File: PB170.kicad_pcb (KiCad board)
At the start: 4 copper layers, 96.5 x 71.1 mm, 39 parts, among them J2 USB_B_Micro, Q1 P-MOSFET-MLP_HS, Q2 BC817, SW1 SW_MEC_5E, SW2 SW_MEC_5E, SW3 SW_SPDT, U1 74HC00, U2 74HC08, U3 74HC4511D, U4 HEF4518BT, U5 74HC32

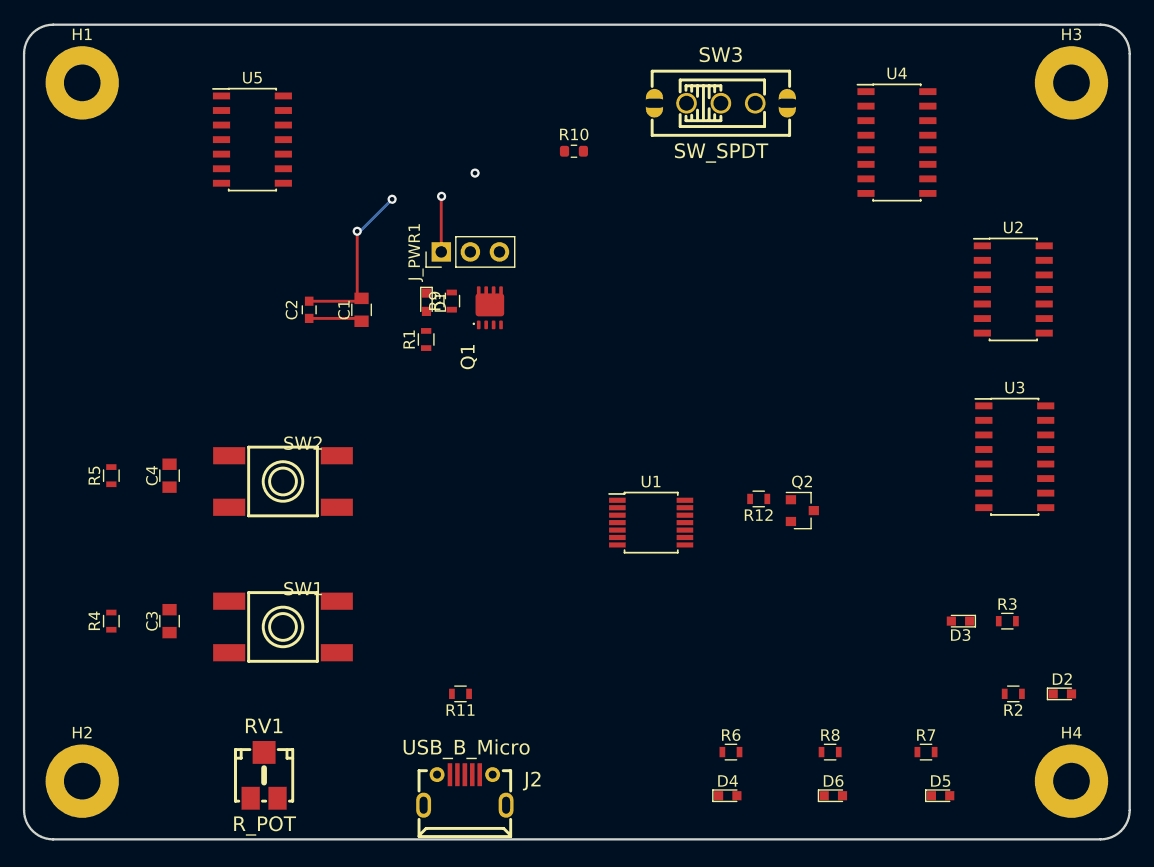
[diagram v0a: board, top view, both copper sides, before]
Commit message: Put components on board, set up 3d models of button and switch
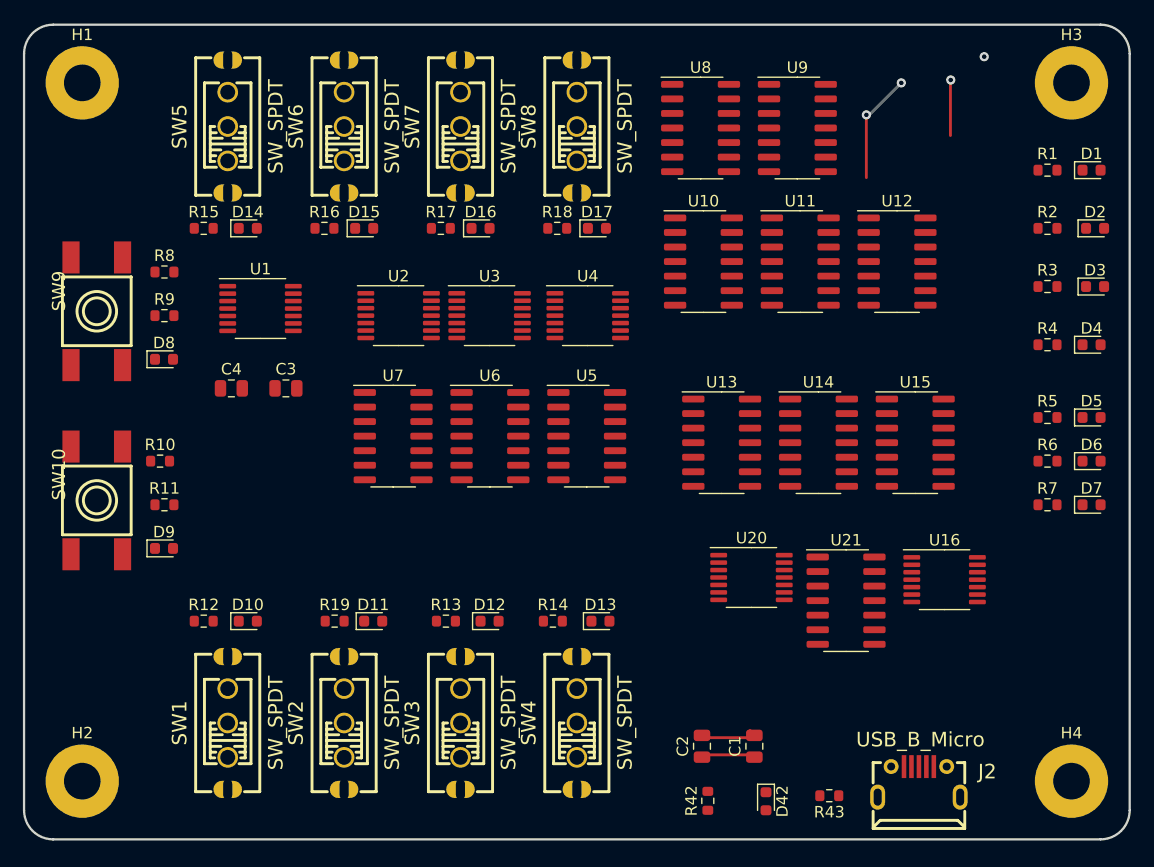
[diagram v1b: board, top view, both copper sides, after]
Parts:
- removed J_PWR1: Conn_01x03, Pin_Headers:Pin_Header_Straight_1x03_Pitch2.54mm
- removed Q1: P-MOSFET-MLP_HS, PB170:MLP3.3X3.3_HS
- removed Q2: BC817, TO_SOT_Packages_SMD:SOT-23
- removed RV1: R_POT, PB170:potentiometer10k
- added D1: LED green, LED_SMD:LED_0603_1608Metric, F.Cu at (133.8, 38.1)
- added D10: LED green, LED_SMD:LED_0603_1608Metric, F.Cu at (60.2, 77.5)
- added D11: LED green, LED_SMD:LED_0603_1608Metric, F.Cu at (71.1, 77.5)
- added D12: LED green, LED_SMD:LED_0603_1608Metric, F.Cu at (81.3, 77.5)
- added D13: LED green, LED_SMD:LED_0603_1608Metric, F.Cu at (91.0, 77.5)
- added D14: LED green, LED_SMD:LED_0603_1608Metric, F.Cu at (60.2, 43.2)
- added D15: LED green, LED_SMD:LED_0603_1608Metric, F.Cu at (70.3, 43.2)
- added D16: LED green, LED_SMD:LED_0603_1608Metric, F.Cu at (80.5, 43.2)
- added D17: LED green, LED_SMD:LED_0603_1608Metric, F.Cu at (90.7, 43.2)
- added D7: LED yellow, LED_SMD:LED_0603_1608Metric, F.Cu at (133.8, 67.3)
- added D8: LED yellow, LED_SMD:LED_0603_1608Metric, F.Cu at (52.9, 54.6)
- added D9: LED yellow, LED_SMD:LED_0603_1608Metric, F.Cu at (52.9, 71.1)
- added R1: 180R, Resistor_SMD:R_0603_1608Metric, F.Cu at (130.0, 38.1)
- added R11: 180R, Resistor_SMD:R_0603_1608Metric, F.Cu at (52.9, 67.3)
- added R13: 180R, Resistor_SMD:R_0603_1608Metric, F.Cu at (77.5, 77.5)
- added R14: 180R, Resistor_SMD:R_0603_1608Metric, F.Cu at (86.8, 77.5)
- added R15: 180R, Resistor_SMD:R_0603_1608Metric, F.Cu at (56.3, 43.2)
- added R16: 180R, Resistor_SMD:R_0603_1608Metric, F.Cu at (66.9, 43.2)
- added R17: 180R, Resistor_SMD:R_0603_1608Metric, F.Cu at (77.0, 43.2)
- added R18: 180R, Resistor_SMD:R_0603_1608Metric, F.Cu at (87.2, 43.2)
- added R19: 180R, Resistor_SMD:R_0603_1608Metric, F.Cu at (67.8, 77.5)
- added SW10: SW_MEC_5E, PB170:TactileSwitch_C381064, F.Cu at (47.0, 66.9)
- added SW4: SW_SPDT, PB170:toggleSwitch, F.Cu at (88.9, 86.4)
- added SW5: SW_SPDT, PB170:toggleSwitch, F.Cu at (58.4, 34.3)
- added SW6: SW_SPDT, PB170:toggleSwitch, F.Cu at (68.6, 34.3)
- added SW7: SW_SPDT, PB170:toggleSwitch, F.Cu at (78.7, 34.3)
- added SW8: SW_SPDT, PB170:toggleSwitch, F.Cu at (88.9, 34.3)
- added SW9: SW_MEC_5E, PB170:TactileSwitch_C381064, F.Cu at (47.0, 50.4)
- added U10: 74HC08, Package_SO:SOIC-14_3.9x8.7mm_P1.27mm, F.Cu at (100.0, 46.1)
- added U11: 74HC08, Package_SO:SOIC-14_3.9x8.7mm_P1.27mm, F.Cu at (108.4, 46.1)
- added U12: 74HC32, Package_SO:SOIC-14_3.9x8.7mm_P1.27mm, F.Cu at (116.8, 46.1)
- added U13: 74HC08, Package_SO:SOIC-14_3.9x8.7mm_P1.27mm, F.Cu at (101.5, 61.9)
- added U14: 74HC08, Package_SO:SOIC-14_3.9x8.7mm_P1.27mm, F.Cu at (110.0, 61.9)
- added U15: 74HC32, Package_SO:SOIC-14_3.9x8.7mm_P1.27mm, F.Cu at (118.4, 61.9)
- added U16: 74HC86, Package_SO:TSSOP-14_4.4x5mm_P0.65mm, F.Cu at (121.0, 73.8)
- added U20: 74HC00, Package_SO:TSSOP-14_4.4x5mm_P0.65mm, F.Cu at (104.1, 73.7)
- added U21: 74HC32, Package_SO:SOIC-14_3.9x8.7mm_P1.27mm, F.Cu at (112.4, 75.7)
- added U6: 74HC08, Package_SO:SOIC-14_3.9x8.7mm_P1.27mm, F.Cu at (81.3, 61.3)
- added U7: 74HC32, Package_SO:SOIC-14_3.9x8.7mm_P1.27mm, F.Cu at (72.9, 61.3)
- added U8: 74HC08, Package_SO:SOIC-14_3.9x8.7mm_P1.27mm, F.Cu at (99.7, 34.4)
- added U9: 74HC32, Package_SO:SOIC-14_3.9x8.7mm_P1.27mm, F.Cu at (108.2, 34.4)
- C1, C3, C4: footprint Capacitors_SMD:C_0805 -> Capacitor_SMD:C_0805_2012Metric
- C2: footprint Capacitors_SMD:C_0603 -> Capacitor_SMD:C_0805_2012Metric
- D2, D3: value LED yellow -> LED green; footprint LEDs:LED_0603 -> LED_SMD:LED_0603_1608Metric
- D4: footprint LEDs:LED_0603 -> LED_SMD:LED_0603_1608Metric
- D42: renamed from D1; footprint LEDs:LED_0603 -> LED_SMD:LED_0603_1608Metric
- D5: value LED blue -> LED red; footprint LEDs:LED_0603 -> LED_SMD:LED_0603_1608Metric
- D6: value LED white -> LED yellow; footprint LEDs:LED_0603 -> LED_SMD:LED_0603_1608Metric
- R12, R7: value 220R -> 180R; footprint Resistors_SMD:R_0603 -> Resistor_SMD:R_0603_1608Metric
- R2, R3, R6: footprint Resistors_SMD:R_0603 -> Resistor_SMD:R_0603_1608Metric
- R4, R9: value 10k -> 180R; footprint Resistors_SMD:R_0603 -> Resistor_SMD:R_0603_1608Metric
- R42: renamed from R1; footprint Resistors_SMD:R_0603 -> Resistor_SMD:R_0603_1608Metric
- R43: renamed from R11; footprint Resistors_SMD:R_0603 -> Resistor_SMD:R_0603_1608Metric
- R5: value 10k -> 220R; footprint Resistors_SMD:R_0603 -> Resistor_SMD:R_0603_1608Metric
- R8: value 130R -> 10k; footprint Resistors_SMD:R_0603 -> Resistor_SMD:R_0603_1608Metric
- SW1, SW2: value SW_MEC_5E -> SW_SPDT; footprint PB170:TactileSwitch_C381064 -> PB170:toggleSwitch
- U1: value 74HC00 -> 74HC74; footprint Housings_SSOP:TSSOP-14_4.4x5mm_Pitch0.65mm -> Package_SO:TSSOP-14_4.4x5mm_P0.65mm
- U2: value 74HC08 -> 74HC86; footprint Housings_SOIC:SOIC-14_3.9x8.7mm_Pitch1.27mm -> Package_SO:TSSOP-14_4.4x5mm_P0.65mm
- U3: value 74HC4511D -> 74HC86; footprint Housings_SOIC:SOIC-16_3.9x9.9mm_Pitch1.27mm -> Package_SO:TSSOP-14_4.4x5mm_P0.65mm
- U4: value HEF4518BT -> 74HC86; footprint Housings_SOIC:SOIC-16_3.9x9.9mm_Pitch1.27mm -> Package_SO:TSSOP-14_4.4x5mm_P0.65mm
- U5: value 74HC32 -> 74HC08; footprint Housings_SOIC:SOIC-14_3.9x8.7mm_Pitch1.27mm -> Package_SO:SOIC-14_3.9x8.7mm_P1.27mm
- moved R4 85.2 mm to (130.0, 53.3), turned to 0 degrees
- moved R5 81.9 mm to (130.0, 59.7), turned to 0 degrees
- moved R8 71.7 mm to (52.9, 47.0)
- moved SW3 58.7 mm to (78.7, 86.4), turned to 90 degrees
- moved U2 53.7 mm to (73.3, 50.8)
- moved D42 52.7 mm to (105.4, 93.2)
- moved C1 51.3 mm to (104.4, 88.4)
- moved C2 51.3 mm to (99.8, 88.4)
- moved D4 50.6 mm to (133.8, 53.3)
- moved R12 49.6 mm to (56.3, 77.5), turned to 0 degrees
- moved U3 47.5 mm to (81.3, 50.8)
- moved R42 47.2 mm to (100.3, 93.2)
- moved R10 45.1 mm to (52.5, 63.5)
- moved R2 40.7 mm to (130.0, 43.2), turned to 0 degrees
- moved D2 40.7 mm to (134.1, 43.2)
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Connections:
- C3 pad 1: /SheetXOR/IN_A -> Net-(C3-Pad1)
- C4 pad 1: /SheetXOR/IN_B -> Net-(C4-Pad1)
- D2 pad 2: /SheetXOR/IN_A -> /SheetOutput/IN_Y1
- D3 pad 2: /SheetXOR/IN_B -> /SheetOutput/IN_Y2
- D4 pad 2: Net-(D4-Pad2) -> /SheetOutput/IN_NF
- D5 pad 2: Net-(D4-Pad2) -> /SheetOutput/IN_OF
- D6 pad 2: Net-(D4-Pad2) -> /SheetOutput/IN_NF
- R10 pad 1: Net-(R10-Pad1) -> Net-(C4-Pad1)
- R12 pad 2: OUTPUT -> GND
- R4 pad 1: /SheetXOR/IN_A -> Net-(D4-Pad1)
- R5 pad 1: /SheetXOR/IN_B -> Net-(D5-Pad1)
- R6 pad 1: Net-(D4-Pad1) -> Net-(D6-Pad1)
- R7 pad 1: Net-(D5-Pad1) -> Net-(D7-Pad1)
- R8 pad 1: Net-(D6-Pad1) -> Net-(C3-Pad1)
- SW1 pad 2: +5V -> /SheetALU/IN_A0
- SW1 pad 3: /SheetXOR/IN_A -> GND
- SW1 pad 4: /SheetXOR/IN_A -> (no net)
- SW2 pad 2: +5V -> /SheetALU/IN_A1
- SW2 pad 3: /SheetXOR/IN_B -> GND
- SW2 pad 4: /SheetXOR/IN_B -> (no net)
- SW3 pad 2: Net-(SW3-Pad2) -> /SheetALU/IN_A2
- U1 pad 1: /SheetXOR/IN_A -> GND
- U1 pad 10: /SheetXOR/IN_B -> GND
- U1 pad 11: OUTPUT -> Net-(C4-Pad1)
- U1 pad 13: Net-(U1-Pad13) -> GND
- U1 pad 2: /SheetXOR/IN_B -> Net-(U1-Pad2)
- U1 pad 3: Net-(U1-Pad3) -> Net-(C3-Pad1)
- U1 pad 4: /SheetXOR/IN_A -> GND
- U1 pad 5: Net-(U1-Pad3) -> /SheetALU/IN_OP0
- U1 pad 6: Net-(U1-Pad12) -> Net-(U1-Pad2)
- U1 pad 8: Net-(U1-Pad13) -> Net-(U1-Pad12)
- U1 pad 9: Net-(U1-Pad3) -> /SheetALU/IN_OP1
- U2 pad 1: Net-(U2-Pad1) -> /SheetALU/IN_OP0
- U2 pad 10: Net-(U2-Pad10) -> /SheetALU/IN_B2
- U2 pad 12: Net-(U2-Pad12) -> /SheetALU/IN_OP0
- U2 pad 13: Net-(U2-Pad13) -> /SheetALU/IN_B3
- U2 pad 2: Net-(U2-Pad2) -> /SheetALU/IN_B0
- U2 pad 4: Net-(U2-Pad4) -> /SheetALU/IN_OP0
- U2 pad 5: Net-(U2-Pad5) -> /SheetALU/IN_B1
- U2 pad 9: Net-(U2-Pad9) -> /SheetALU/IN_OP0
- U3 pad 1: Net-(U3-Pad1) -> /SheetALU/IN_A0
- U3 pad 10: Net-(U3-Pad10) -> Net-(U2-Pad6)
- U3 pad 11: Net-(U3-Pad11) -> /SheetALU/SheetOperationMux/IN_A1
- U3 pad 14: Net-(U3-Pad14) -> +5V
- U3 pad 2: Net-(U3-Pad2) -> Net-(U2-Pad3)
- U3 pad 4: Net-(U3-Pad4) -> Net-(U3-Pad3)
- U3 pad 5: Net-(U3-Pad5) -> /SheetALU/IN_OP0
- U3 pad 6: Net-(U3-Pad6) -> /SheetALU/SheetOperationMux/IN_A0
- U3 pad 7: Net-(U3-Pad7) -> GND
- U3 pad 8: GND -> Net-(U3-Pad12)
- U3 pad 9: Net-(U3-Pad9) -> /SheetALU/IN_A1
- U4 pad 1: Net-(U4-Pad1) -> /SheetALU/IN_A2
- U4 pad 10: Net-(U4-Pad10) -> Net-(U2-Pad11)
- U4 pad 11: Net-(U4-Pad11) -> /SheetALU/SheetOperationMux/IN_A3
- U4 pad 14: Net-(U4-Pad14) -> +5V
- U4 pad 2: Net-(U4-Pad2) -> Net-(U2-Pad8)
- U4 pad 4: Net-(U4-Pad4) -> Net-(U4-Pad3)
- U4 pad 6: Net-(U4-Pad6) -> /SheetALU/SheetOperationMux/IN_A2
- U4 pad 7: Net-(U4-Pad7) -> GND
- U4 pad 8: GND -> Net-(U4-Pad12)
- U4 pad 9: Net-(U4-Pad9) -> /SheetALU/IN_A3
- U5 pad 1: Net-(U5-Pad1) -> /SheetALU/IN_OP0
- U5 pad 10: Net-(U5-Pad10) -> Net-(U3-Pad12)
- U5 pad 12: Net-(U5-Pad12) -> Net-(U2-Pad6)
- U5 pad 13: Net-(U5-Pad13) -> /SheetALU/IN_A1
- U5 pad 2: Net-(U5-Pad2) -> Net-(U3-Pad3)
- U5 pad 4: Net-(U5-Pad4) -> Net-(U2-Pad3)
- U5 pad 5: Net-(U5-Pad5) -> /SheetALU/IN_A0
- U5 pad 9: Net-(U5-Pad9) -> Net-(U3-Pad13)

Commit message: Finished routing
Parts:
- moved U20 42.9 mm to (110.7, 31.2), turned to 180 degrees
- moved U16 37.0 mm to (122.2, 36.8)
- moved U11 34.9 mm to (113.0, 80.6)
- moved U9 33.4 mm to (102.2, 67.3), turned to 90 degrees
- moved U21 29.6 mm to (118.1, 46.7), turned to 90 degrees
- moved U4 29.1 mm to (67.3, 69.2), turned to 180 degrees
- moved U14 22.9 mm to (123.0, 80.8)
- moved U12 21.6 mm to (114.6, 67.6), turned to 180 degrees
- moved C4 21.3 mm to (47.0, 74.9), turned to 180 degrees
- moved U8 19.1 mm to (102.2, 53.3), turned to 90 degrees
- moved U13 18.8 mm to (102.9, 80.6)
- moved U7 17.3 mm to (90.2, 61.6), turned to 180 degrees
- moved C3 16.6 mm to (47.0, 58.4), turned to 180 degrees
- moved U3 16.6 mm to (67.3, 59.7), turned to 90 degrees
- moved U10 14.0 mm to (99.3, 32.1)
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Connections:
- U16 pad 10: Net-(U16-Pad10) -> GND
- U16 pad 12: Net-(U16-Pad12) -> GND
- U16 pad 13: Net-(U16-Pad13) -> GND
- U16 pad 9: Net-(U16-Pad9) -> GND
- U21 pad 12: Net-(U21-Pad12) -> GND
- U21 pad 13: Net-(U21-Pad13) -> GND
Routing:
- net GND: track 32.0 -> 514.7 mm, vias 4 -> 45
- net +5V: track 4.68 -> 432.0 mm, vias 0 -> 24
- net /SheetALU/IN_OP1: track 0.00 -> 216.4 mm, vias 0 -> 6
- net /SheetALU/IN_OP0: track 0.00 -> 202.2 mm, vias 0 -> 10
- net /SheetALU/IN_A1: track 0.00 -> 105.6 mm, vias 0 -> 7
- net /SheetALU/IN_A0: track 0.00 -> 104.3 mm, vias 0 -> 6
- net /SheetALU/IN_A3: track 0.00 -> 99.7 mm, vias 0 -> 5
- net /SheetALU/IN_B1: track 0.00 -> 80.6 mm, vias 0 -> 3
- net /SheetALU/IN_A2: track 0.00 -> 79.8 mm, vias 0 -> 3
- net /SheetALU/IN_B0: track 0.00 -> 78.0 mm, vias 0 -> 3
- net /SheetALU/SheetOperationMux/IN_NOT_OP: track 0.00 -> 75.0 mm, vias 0 -> 10
- net Net-(U16-Pad1): track 0.00 -> 73.2 mm, vias 0 -> 5
- net /SheetALU/IN_B2: track 0.00 -> 70.5 mm, vias 0 -> 5
- net Net-(U13-Pad11): track 0.00 -> 67.7 mm, vias 0 -> 2
- net Net-(U13-Pad6): track 0.00 -> 64.0 mm, vias 0 -> 2
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
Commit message: Added labels
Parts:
- moved R42 1.02 mm to (100.3, 92.1)
- moved D42 1.02 mm to (105.4, 92.2)
- moved H2 1.02 mm to (45.7, 90.4)
- moved H4 1.02 mm to (132.1, 90.4)
- moved J2 0.06 mm to (119.4, 92.6)
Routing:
- net /SheetALU/IN_OP1: track 216.4 -> 221.4 mm
- net GND: track 514.7 -> 511.9 mm, vias 45 -> 44
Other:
- board size 96.5 x 71.1 mm -> 96.5 x 70.1 mm
- board text added: "A"
- board text added: "A0"
- board text added: "A1"
- board text added: "A2"
- board text added: "A3"
- board text added: "B"
- board text added: "B0"
- board text added: "B1"
- board text added: "B2"
- board text added: "B3"
- board text added: "NEGATIVE"
- board text added: "OP0"
- board text added: "OP1"
- board text added: "OVERFLOW"
- board text added: "POWER"
- board text added: "Y0"
- board text added: "Y1"
- board text added: "Y2"
- board text added: "Y3"
- board text added: "ZERO"

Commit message: Signature
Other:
- board text added: "Ondrej Klinovský Jakub Maloštík"
